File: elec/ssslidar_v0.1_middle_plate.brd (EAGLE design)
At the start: 15.6 x 18 mm, 6 parts

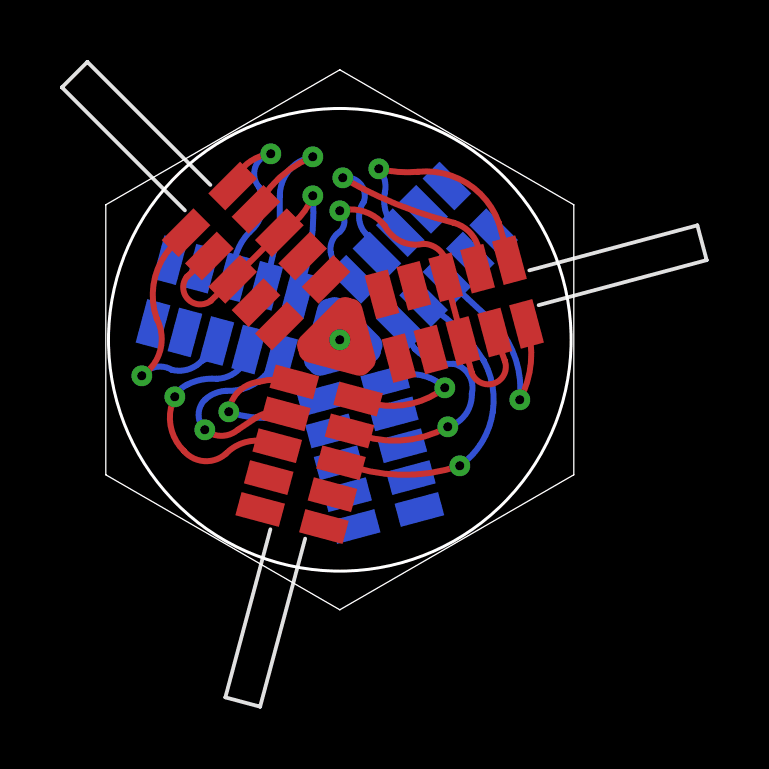
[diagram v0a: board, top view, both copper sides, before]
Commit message: Cosmetic improvements on middle plate
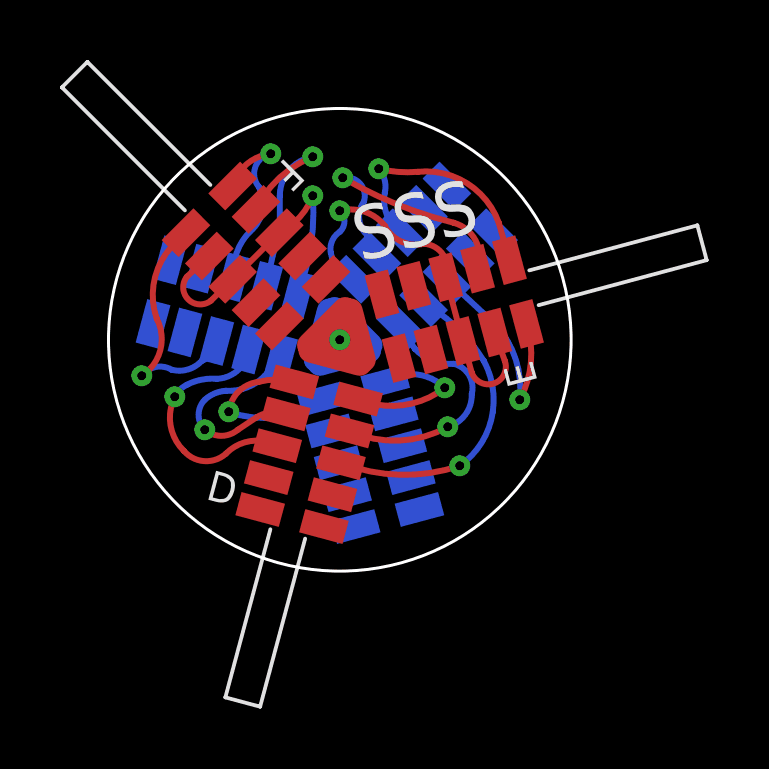
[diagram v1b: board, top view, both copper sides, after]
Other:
- board size 15.6 x 18 mm -> 15.4 x 15.4 mm
- board text added: "D"
- board text added: "E"
- board text added: "F"
- board text added: "SSS"
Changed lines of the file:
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@@
 <board>
 <plain>
-<wire x1="0.2" y1="12.5" x2="0.2" y2="3.5" width="0.01" layer="20"/>
-<wire x1="0.2" y1="3.5" x2="8" y2="-1" width="0.01" layer="20"/>
-<wire x1="8" y1="-1" x2="15.8" y2="3.5" width="0.01" layer="20"/>
-<wire x1="15.8" y1="3.5" x2="15.8" y2="12.5" width="0.01" layer="20"/>
-<wire x1="15.8" y1="12.5" x2="8" y2="17" width="0.01" layer="20"/>
-<wire x1="8" y1="17" x2="0.2" y2="12.5" width="0.01" layer="20"/>
 <circle x="8" y="8" radius="7.71038125" width="0.1" layer="20"/>
+<text x="8.7" y="10.6" size="1.778" layer="21" font="vector" ratio="15" rot="R15">SSS</text>
+<text x="3.5" y="2.7" size="1" layer="21" font="vector" ratio="15" rot="R345">D</text>
+<text x="14.6" y="6.6" size="1" layer="21" font="vector" ratio="15" rot="SR105">E</text>
+<text x="6.2" y="14.1" size="1" layer="21" font="vector" ratio="15" rot="SR225">F</text>
 </plain>
 <attributes>

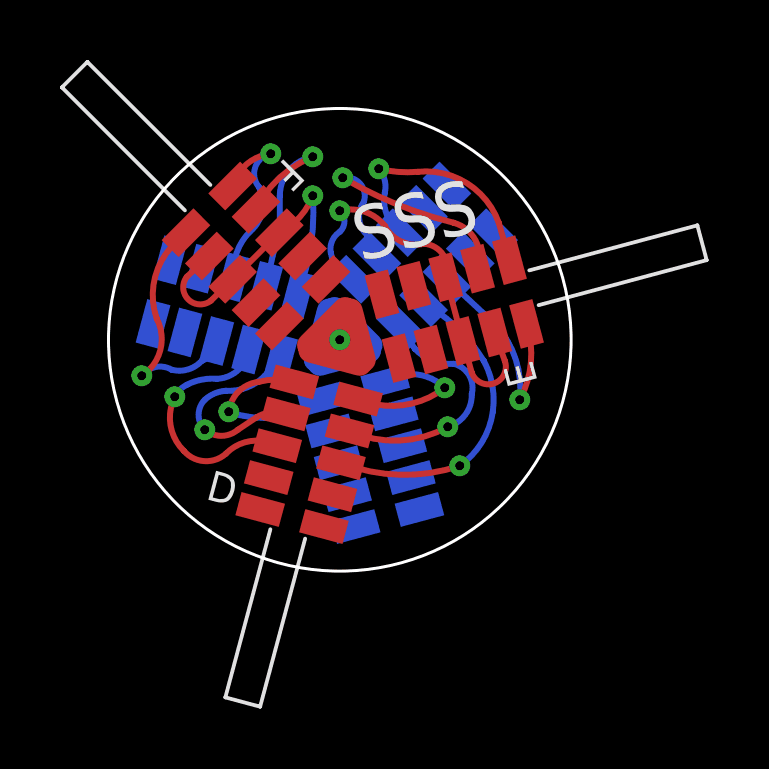
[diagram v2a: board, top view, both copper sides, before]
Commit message: Fixed middle plate with double power rails
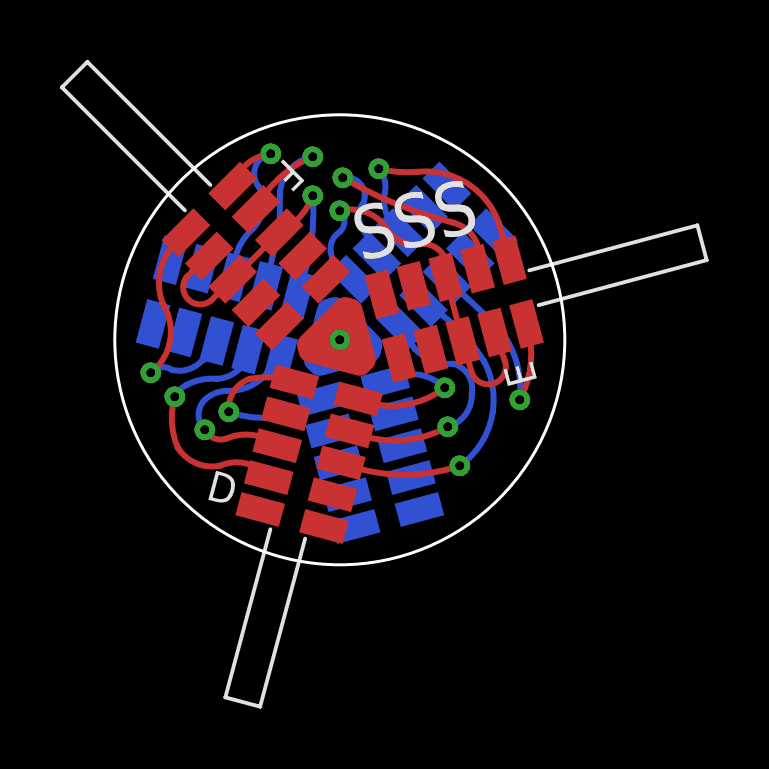
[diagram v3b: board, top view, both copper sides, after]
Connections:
- net N$14: now also B1.4; no longer B1.3
- net N$6: now also B1.5; no longer B1.4
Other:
- board size 15.4 x 15.4 mm -> 15 x 15 mm
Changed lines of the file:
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@@
 <board>
 <plain>
-<circle x="8" y="8" radius="7.71038125" width="0.1" layer="20"/>
+<circle x="8" y="8" radius="7.5" width="0.1" layer="20"/>
 <text x="8.7" y="10.6" size="1.778" layer="21" font="vector" ratio="15" rot="R15">SSS</text>
 <text x="3.5" y="2.7" size="1" layer="21" font="vector" ratio="15" rot="R345">D</text>
@@
 <wire x1="7.390415625" y1="6.024928125" x2="4.3" y2="5.6" width="0.2" layer="16" curve="-55.974559"/>
 <via x="4.3" y="5.6" extent="1-16" drill="0.3"/>
-<wire x1="4.3" y1="5.6" x2="5.3" y2="6.6" width="0.2" layer="1" curve="-77.033827"/>
-<wire x1="5.3" y1="6.6" x2="6.484546875" y2="6.594328125" width="0.2" layer="1" curve="-29.379539"/>
+<wire x1="4.3" y1="5.6" x2="5" y2="6.7" width="0.2" layer="1" curve="-77.033827"/>
+<wire x1="5" y1="6.7" x2="6.484546875" y2="6.594328125" width="0.2" layer="1" curve="-29.379539"/>
 </signal>
 <signal name="N$1">
@@
 <signal name="N$6">
 <contactref element="B6" pad="3"/>
-<contactref element="B1" pad="4"/>
-<wire x1="5.91514375" y1="4.46929375" x2="4.2" y2="4.2" width="0.2" layer="1" curve="74.163437"/>
-<wire x1="4.2" y1="4.2" x2="2.8" y2="4.3" width="0.2" layer="1" curve="-91.287602"/>
-<wire x1="2.8" y1="4.3" x2="2.5" y2="6.1" width="0.2" layer="1" curve="-72.054747"/>
+<contactref element="B1" pad="5"/>
+<wire x1="5.63044375" y1="3.406775" x2="4" y2="3.8" width="0.2" layer="1" curve="74.163437"/>
+<wire x1="4" y1="3.8" x2="2.6" y2="4.4" width="0.2" layer="1" curve="-68.122136"/>
+<wire x1="2.6" y1="4.4" x2="2.5" y2="6.1" width="0.2" layer="1" curve="-39.307648"/>
 <via x="2.5" y="6.1" extent="1-16" drill="0.3"/>
 <wire x1="2.5" y1="6.1" x2="2.9" y2="6.5" width="0.2" layer="16" curve="-36.869898"/>
@@
 <contactref element="B2" pad="7"/>
 <wire x1="2.873475" y1="11.5708875" x2="2.6" y2="11.3" width="0.2" layer="1"/>
-<wire x1="2.6" y1="11.3" x2="1.9" y2="8.7" width="0.2" layer="1" curve="69.01704"/>
-<wire x1="1.9" y1="8.7" x2="1.4" y2="6.8" width="0.2" layer="1" curve="-84.547378"/>
-<via x="1.4" y="6.8" extent="1-16" drill="0.3"/>
-<wire x1="1.4" y1="6.8" x2="2.4" y2="7" width="0.2" layer="16" curve="-84.547378"/>
+<wire x1="2.6" y1="11.3" x2="2.1" y2="9.2" width="0.2" layer="1" curve="69.01704"/>
+<wire x1="2.1" y1="9.2" x2="1.7" y2="6.9" width="0.2" layer="1" curve="-84.547378"/>
+<via x="1.7" y="6.9" extent="1-16" drill="0.3"/>
+<wire x1="1.7" y1="6.9" x2="2.4" y2="7" width="0.2" layer="16" curve="-84.547378"/>
 <wire x1="2.4" y1="7" x2="3.4" y2="7.3" width="0.2" layer="16" curve="61.927455"/>
 <wire x1="3.4" y1="7.3" x2="3.89989375" y2="7.959815625" width="0.2" layer="16" curve="65.628491"/>
@@
 <via x="11.6" y="5.1" extent="1-16" drill="0.3"/>
 <wire x1="11.6" y1="5.1" x2="12.4" y2="6.2" width="0.2" layer="16" curve="76.177424"/>
-<wire x1="12.4" y1="6.2" x2="11.8" y2="7.2" width="0.2" layer="16" curve="90"/>
+<wire x1="12.4" y1="6.2" x2="11.8" y2="7.2" width="0.2" layer="16" curve="83.75562"/>
 <wire x1="11.8" y1="7.2" x2="10.5" y2="7.7" width="0.2" layer="16" curve="-51.11975"/>
 <wire x1="10.5" y1="7.7" x2="10.01525625" y2="8.45961875" width="0.2" layer="16"/>
 </signal>
 <signal name="N$14">
-<contactref element="B1" pad="3"/>
+<contactref element="B1" pad="4"/>
 <contactref element="B6" pad="2"/>
 <wire x1="6.02493125" y1="7.3904125" x2="5.5" y2="6.8" width="0.2" layer="16"/>
@@
 <wire x1="3.5" y1="6" x2="3.5" y2="5" width="0.2" layer="16" curve="90"/>
 <via x="3.5" y="5" extent="1-16" drill="0.3"/>
-<wire x1="3.5" y1="5" x2="4.6" y2="5" width="0.2" layer="1" curve="80.472717"/>
-<wire x1="4.6" y1="5" x2="5.2" y2="5.4" width="0.2" layer="1"/>
-<wire x1="5.2" y1="5.4" x2="6.199846875" y2="5.531809375" width="0.2" layer="1" curve="-52.407106"/>
+<wire x1="3.5" y1="5" x2="4.2" y2="4.7" width="0.2" layer="1" curve="80.472717"/>
+<wire x1="4.2" y1="4.7" x2="4.5" y2="4.8" width="0.2" layer="1"/>
+<wire x1="4.5" y1="4.8" x2="5.91514375" y2="4.46929375" width="0.2" layer="1" curve="-52.407106"/>
 </signal>
 <signal name="N$21">
